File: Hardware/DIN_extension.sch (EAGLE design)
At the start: 7 parts, among them X1 MAB5SH, X2 MAB5SH

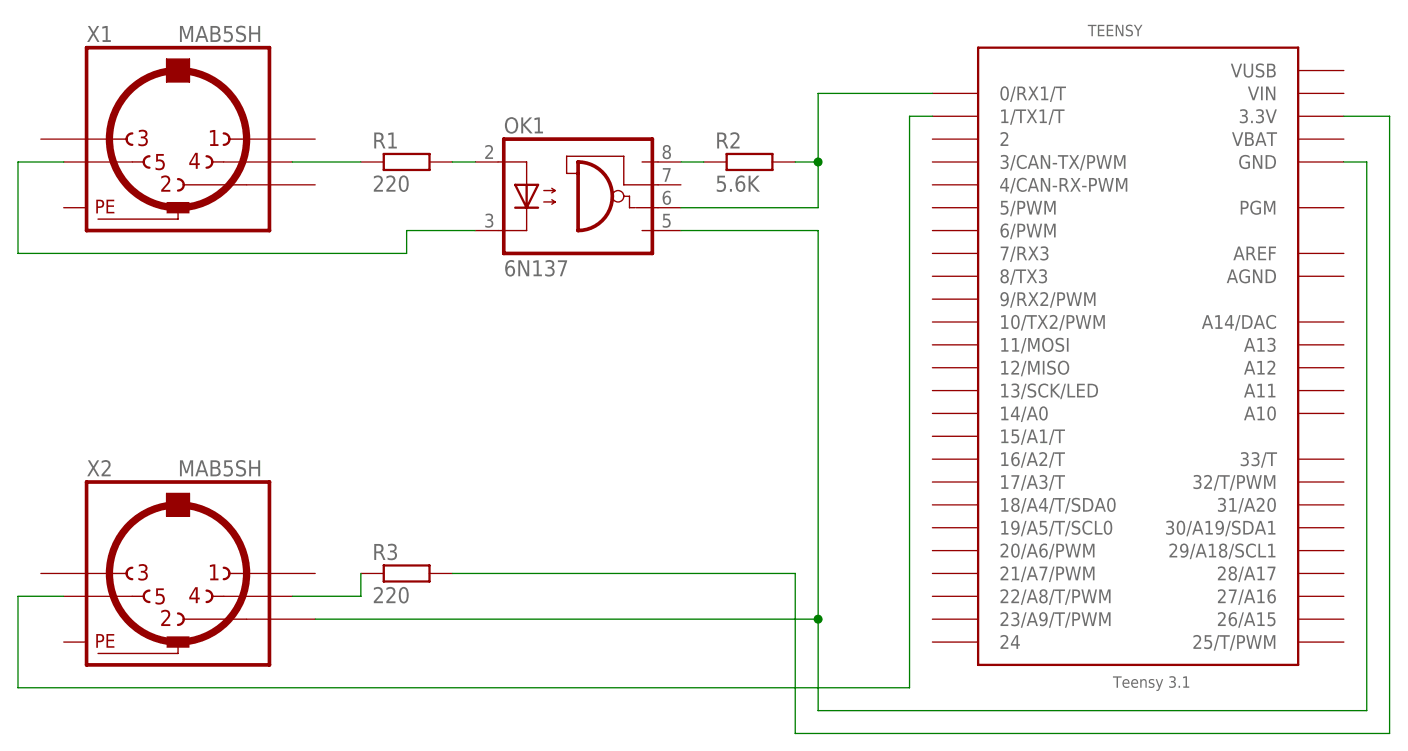
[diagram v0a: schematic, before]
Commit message: version 1.0.1
bugfix in the DIN extension schematic
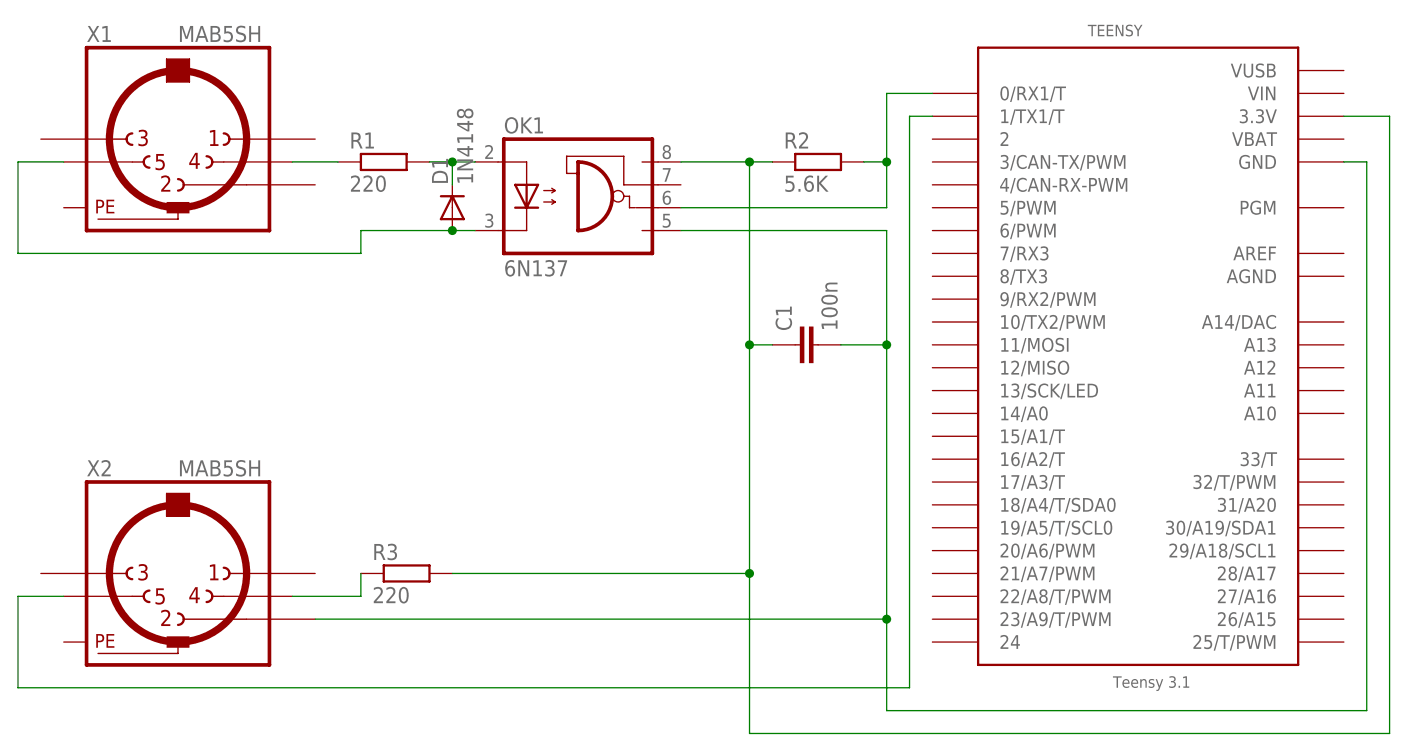
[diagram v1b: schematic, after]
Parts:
- added C1: 100n, resistor:C-EU025-024X044
- added D1: 1N4148, diode:1N4148DO35-7
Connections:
- removed net N$10: R3.2, TEENSY.3.3V
- net N$2: now also D1.C
- net N$3: now also C1.1, R3.2, TEENSY.3.3V
- net N$6: now also D1.A
- net N$7: now also C1.2
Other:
- moved on the sheet: R1, R2
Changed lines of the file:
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@@
 <part name="X2" library="con-hirschmann" deviceset="MAB5SH" device=""/>
 <part name="OK1" library="optocoupler" deviceset="6N137" device=""/>
+<part name="D1" library="diode" deviceset="1N4148" device="DO35-7" value="1N4148"/>
+<part name="C1" library="resistor" deviceset="C-EU" device="025-024X044" value="100n"/>
 </parts>
 <sheets>
@@
 </plain>
 <instances>
-<instance part="R1" gate="G$1" x="30.48" y="68.58"/>
-<instance part="R2" gate="G$1" x="68.58" y="68.58"/>
+<instance part="R1" gate="G$1" x="27.94" y="68.58"/>
+<instance part="R2" gate="G$1" x="76.2" y="68.58"/>
 <instance part="R3" gate="G$1" x="30.48" y="22.86"/>
 <instance part="TEENSY" gate="G$1" x="111.76" y="48.26"/>
@@
 <instance part="X2" gate="G$1" x="5.08" y="22.86"/>
 <instance part="OK1" gate="A" x="50.8" y="63.5"/>
+<instance part="D1" gate="G$1" x="35.56" y="63.5" rot="R90"/>
+<instance part="C1" gate="G$1" x="73.66" y="48.26" rot="R90"/>
 </instances>
 <busses>
@@
 <pinref part="X1" gate="G$1" pin="4"/>
 <pinref part="R1" gate="G$1" pin="1"/>
-<wire x1="17.78" y1="68.58" x2="25.4" y2="68.58" width="0.1524" layer="91"/>
+<wire x1="17.78" y1="68.58" x2="22.86" y2="68.58" width="0.1524" layer="91"/>
 </segment>
 </net>
@@
 <pinref part="R1" gate="G$1" pin="2"/>
 <pinref part="OK1" gate="A" pin="A"/>
+<wire x1="33.02" y1="68.58" x2="35.56" y2="68.58" width="0.1524" layer="91"/>
+<pinref part="D1" gate="G$1" pin="C"/>
 <wire x1="35.56" y1="68.58" x2="38.1" y2="68.58" width="0.1524" layer="91"/>
+<wire x1="35.56" y1="66.04" x2="35.56" y2="68.58" width="0.1524" layer="91"/>
+<junction x="35.56" y="68.58"/>
 </segment>
 </net>
@@
 <pinref part="OK1" gate="A" pin="VCC"/>
 <pinref part="R2" gate="G$1" pin="1"/>
-<wire x1="60.96" y1="68.58" x2="63.5" y2="68.58" width="0.1524" layer="91"/>
+<wire x1="60.96" y1="68.58" x2="68.58" y2="68.58" width="0.1524" layer="91"/>
+<pinref part="R3" gate="G$1" pin="2"/>
+<wire x1="68.58" y1="68.58" x2="71.12" y2="68.58" width="0.1524" layer="91"/>
+<wire x1="35.56" y1="22.86" x2="68.58" y2="22.86" width="0.1524" layer="91"/>
+<wire x1="68.58" y1="22.86" x2="68.58" y2="5.08" width="0.1524" layer="91"/>
+<wire x1="68.58" y1="5.08" x2="139.7" y2="5.08" width="0.1524" layer="91"/>
+<wire x1="139.7" y1="5.08" x2="139.7" y2="73.66" width="0.1524" layer="91"/>
+<pinref part="TEENSY" gate="G$1" pin="3.3V"/>
+<wire x1="139.7" y1="73.66" x2="134.62" y2="73.66" width="0.1524" layer="91"/>
+<wire x1="68.58" y1="68.58" x2="68.58" y2="48.26" width="0.1524" layer="91"/>
+<junction x="68.58" y="68.58"/>
+<junction x="68.58" y="22.86"/>
+<pinref part="C1" gate="G$1" pin="1"/>
+<wire x1="68.58" y1="48.26" x2="68.58" y2="22.86" width="0.1524" layer="91"/>
+<wire x1="71.12" y1="48.26" x2="68.58" y2="48.26" width="0.1524" layer="91"/>
+<junction x="68.58" y="48.26"/>
 </segment>
 </net>
@@
 <wire x1="-7.62" y1="68.58" x2="-12.7" y2="68.58" width="0.1524" layer="91"/>
 <wire x1="-12.7" y1="68.58" x2="-12.7" y2="58.42" width="0.1524" layer="91"/>
-<wire x1="-12.7" y1="58.42" x2="30.48" y2="58.42" width="0.1524" layer="91"/>
-<wire x1="30.48" y1="58.42" x2="30.48" y2="60.96" width="0.1524" layer="91"/>
+<wire x1="-12.7" y1="58.42" x2="25.4" y2="58.42" width="0.1524" layer="91"/>
+<wire x1="25.4" y1="58.42" x2="25.4" y2="60.96" width="0.1524" layer="91"/>
 <pinref part="OK1" gate="A" pin="C"/>
-<wire x1="30.48" y1="60.96" x2="38.1" y2="60.96" width="0.1524" layer="91"/>
+<wire x1="25.4" y1="60.96" x2="35.56" y2="60.96" width="0.1524" layer="91"/>
+<pinref part="D1" gate="G$1" pin="A"/>
+<wire x1="35.56" y1="60.96" x2="38.1" y2="60.96" width="0.1524" layer="91"/>
+<junction x="35.56" y="60.96"/>
 </segment>
 </net>
 <net name="N$7" class="0">
 <segment>
-<wire x1="76.2" y1="7.62" x2="137.16" y2="7.62" width="0.1524" layer="91"/>
+<wire x1="83.82" y1="7.62" x2="137.16" y2="7.62" width="0.1524" layer="91"/>
 <wire x1="137.16" y1="7.62" x2="137.16" y2="68.58" width="0.1524" layer="91"/>
 <pinref part="TEENSY" gate="G$1" pin="GND"/>
 <wire x1="137.16" y1="68.58" x2="134.62" y2="68.58" width="0.1524" layer="91"/>
-<wire x1="76.2" y1="7.62" x2="76.2" y2="17.78" width="0.1524" layer="91"/>
+<wire x1="83.82" y1="7.62" x2="83.82" y2="17.78" width="0.1524" layer="91"/>
 <pinref part="OK1" gate="A" pin="GND"/>
-<wire x1="76.2" y1="17.78" x2="76.2" y2="60.96" width="0.1524" layer="91"/>
-<wire x1="76.2" y1="60.96" x2="60.96" y2="60.96" width="0.1524" layer="91"/>
+<wire x1="83.82" y1="17.78" x2="83.82" y2="48.26" width="0.1524" layer="91"/>
+<wire x1="83.82" y1="48.26" x2="83.82" y2="60.96" width="0.1524" layer="91"/>
+<wire x1="83.82" y1="60.96" x2="60.96" y2="60.96" width="0.1524" layer="91"/>
 <pinref part="X2" gate="G$1" pin="2"/>
-<wire x1="20.32" y1="17.78" x2="76.2" y2="17.78" width="0.1524" layer="91"/>
-<junction x="76.2" y="17.78"/>
+<wire x1="20.32" y1="17.78" x2="83.82" y2="17.78" width="0.1524" layer="91"/>
+<junction x="83.82" y="17.78"/>
+<pinref part="C1" gate="G$1" pin="2"/>
+<wire x1="78.74" y1="48.26" x2="83.82" y2="48.26" width="0.1524" layer="91"/>
+<junction x="83.82" y="48.26"/>
 </segment>
 </net>
@@
 <segment>
 <pinref part="OK1" gate="A" pin="VO"/>
-<wire x1="60.96" y1="63.5" x2="76.2" y2="63.5" width="0.1524" layer="91"/>
+<wire x1="60.96" y1="63.5" x2="83.82" y2="63.5" width="0.1524" layer="91"/>
 <pinref part="R2" gate="G$1" pin="2"/>
-<wire x1="73.66" y1="68.58" x2="76.2" y2="68.58" width="0.1524" layer="91"/>
-<wire x1="76.2" y1="68.58" x2="76.2" y2="76.2" width="0.1524" layer="91"/>
+<wire x1="81.28" y1="68.58" x2="83.82" y2="68.58" width="0.1524" layer="91"/>
+<wire x1="83.82" y1="68.58" x2="83.82" y2="76.2" width="0.1524" layer="91"/>
 <pinref part="TEENSY" gate="G$1" pin="0/RX1/T"/>
-<wire x1="76.2" y1="76.2" x2="88.9" y2="76.2" width="0.1524" layer="91"/>
-<wire x1="76.2" y1="63.5" x2="76.2" y2="68.58" width="0.1524" layer="91"/>
-<junction x="76.2" y="68.58"/>
+<wire x1="83.82" y1="76.2" x2="88.9" y2="76.2" width="0.1524" layer="91"/>
+<wire x1="83.82" y1="63.5" x2="83.82" y2="68.58" width="0.1524" layer="91"/>
+<junction x="83.82" y="68.58"/>
 </segment>
 </net>
@@
 </segment>
 </net>
-<net name="N$10" class="0">
-<segment>
-<pinref part="R3" gate="G$1" pin="2"/>
-<wire x1="35.56" y1="22.86" x2="73.66" y2="22.86" width="0.1524" layer="91"/>
-<wire x1="73.66" y1="22.86" x2="73.66" y2="5.08" width="0.1524" layer="91"/>
-<wire x1="73.66" y1="5.08" x2="139.7" y2="5.08" width="0.1524" layer="91"/>
-<wire x1="139.7" y1="5.08" x2="139.7" y2="73.66" width="0.1524" layer="91"/>
-<pinref part="TEENSY" gate="G$1" pin="3.3V"/>
-<wire x1="139.7" y1="73.66" x2="134.62" y2="73.66" width="0.1524" layer="91"/>
-</segment>
-</net>
